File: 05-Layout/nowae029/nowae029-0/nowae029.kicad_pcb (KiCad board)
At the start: 2 copper layers, 100 x 99.9 mm, 160 parts, among them P101 COMM_3, P102 SUPPLY_3, P103 COMM_4, P104 SUPPLY_4, P201 DEBUG, P401 BATTERY, P501 632722110112, P502 UART, Q701 BCW68GLT1G, U201 STM32L073CBT6, U301 TCA9554PWR, U302 TCA9554PWR, U401 TLV70233DBV, U501 FT230XS, U601 TCA9554PWR, U602 TCA9554PWR, Y201 32768

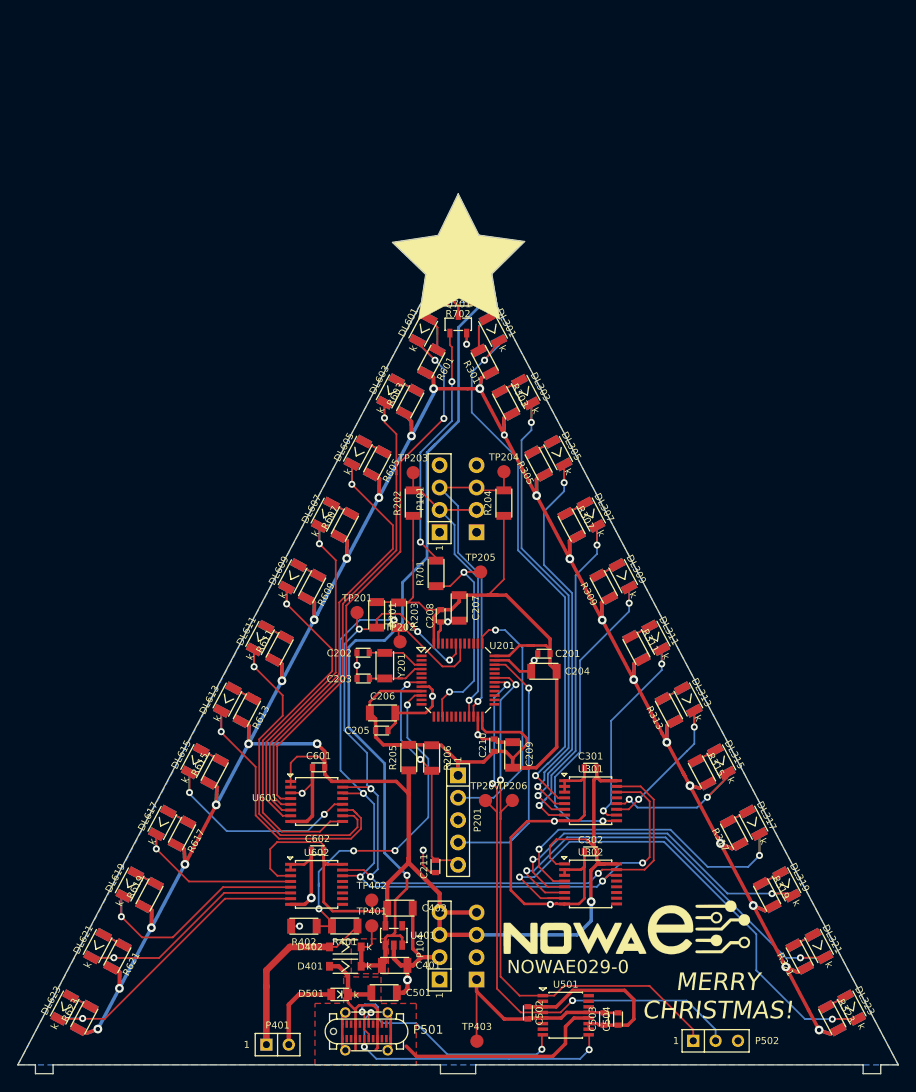
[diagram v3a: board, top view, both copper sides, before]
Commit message: Added fiducial marker
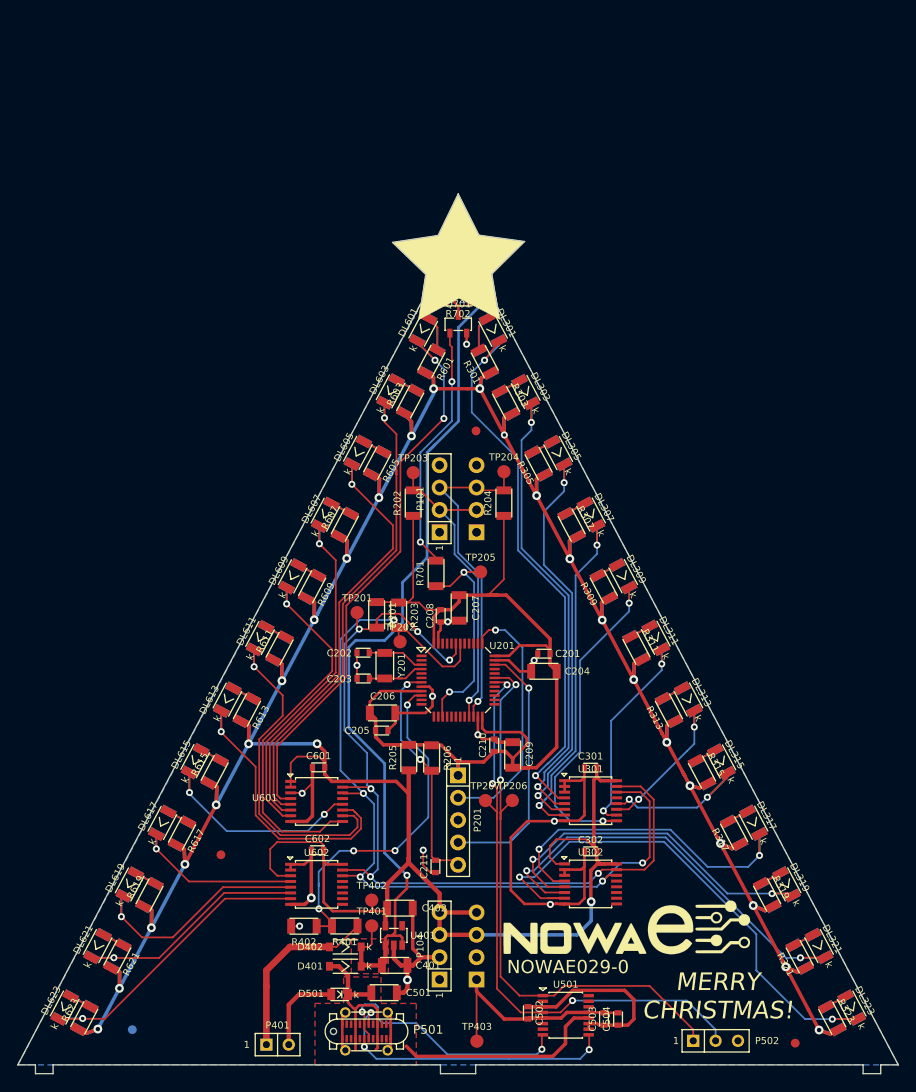
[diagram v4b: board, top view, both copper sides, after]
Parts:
- added VAL**: FIDUCIALMARK_1MM_3MM, MECHANICAL:FIDUCIALMARK_1MM_3MM, B.Cu at (63.0, 145.0)
- added VAL**: FIDUCIALMARK_1MM_3MM, MECHANICAL:FIDUCIALMARK_1MM_3MM, F.Cu at (102.0, 77.0)
- added VAL**: FIDUCIALMARK_1MM_3MM, MECHANICAL:FIDUCIALMARK_1MM_3MM, F.Cu at (73.1, 125.1)
- added VAL**: FIDUCIALMARK_1MM_3MM, MECHANICAL:FIDUCIALMARK_1MM_3MM, F.Cu at (138.3, 146.5)
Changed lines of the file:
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@@
     (tracks 1165)
     (zones 0)
-    (modules 160)
+    (modules 164)
     (nets 156)
   )
@@
     (add_net "Net-(U602-Pad13)")
   )
+  (module MECHANICAL:FIDUCIALMARK_1MM_3MM (layer B.Cu)
+    (at 63 145)
+    (descr "Fiducial Copper Top 1mm copper, 3mm mask")
+    (attr virtual)
+    (fp_text reference VAL** (at 0 2.05) (layer B.SilkS) hide
+      (effects (font (size 0.8 0.8) (thickness 0.15)) (justify mirror))
+    )
+    (fp_text value FIDUCIALMARK_1MM_3MM (at 0 -2.15) (layer B.Fab) hide
+      (effects (font (size 0.8 0.8) (thickness 0.15)) (justify mirror))
+    )
+    (pad "" smd circle (at 0 0) (size 1 1) (layers B.Cu))
+    (pad 1 smd circle (at 0 0) (size 3 3) (layers B.Mask))
+  )
+  (module MECHANICAL:FIDUCIALMARK_1MM_3MM (layer F.Cu)
+    (at 102.04 77)
+    (descr "Fiducial Copper Top 1mm copper, 3mm mask")
+    (attr virtual)
+    (fp_text reference VAL** (at 0 -2.05) (layer F.SilkS) hide
+      (effects (font (size 0.8 0.8) (thickness 0.15)))
+    )
+    (fp_text value FIDUCIALMARK_1MM_3MM (at 0 2.15) (layer F.Fab) hide
+      (effects (font (size 0.8 0.8) (thickness 0.15)))
+    )
+    (pad "" smd circle (at 0 0) (size 1 1) (layers F.Cu))
+    (pad 1 smd circle (at 0 0) (size 3 3) (layers F.Mask))
+  )
+  (module MECHANICAL:FIDUCIALMARK_1MM_3MM (layer F.Cu)
+    (at 73.07 125.14)
+    (descr "Fiducial Copper Top 1mm copper, 3mm mask")
+    (attr virtual)
+    (fp_text reference VAL** (at 0 -2.05) (layer F.SilkS) hide
+      (effects (font (size 0.8 0.8) (thickness 0.15)))
+    )
+    (fp_text value FIDUCIALMARK_1MM_3MM (at 0 2.15) (layer F.Fab) hide
+      (effects (font (size 0.8 0.8) (thickness 0.15)))
+    )
+    (pad "" smd circle (at 0 0) (size 1 1) (layers F.Cu))
+    (pad 1 smd circle (at 0 0) (size 3 3) (layers F.Mask))
+  )
+  (module MECHANICAL:FIDUCIALMARK_1MM_3MM (layer F.Cu)
+    (at 138.29 146.53)
+    (descr "Fiducial Copper Top 1mm copper, 3mm mask")
+    (attr virtual)
+    (fp_text reference VAL** (at 0 -2.05) (layer F.SilkS) hide
+      (effects (font (size 0.8 0.8) (thickness 0.15)))
+    )
+    (fp_text value FIDUCIALMARK_1MM_3MM (at 0 2.15) (layer F.Fab) hide
+      (effects (font (size 0.8 0.8) (thickness 0.15)))
+    )
+    (pad "" smd circle (at 0 0) (size 1 1) (layers F.Cu))
+    (pad 1 smd circle (at 0 0) (size 3 3) (layers F.Mask))
+  )
   (module LOGO:LOGO_NOWAE_30MM_FSILK (layer F.Cu)

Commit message: PCB End! TODO: production documents.
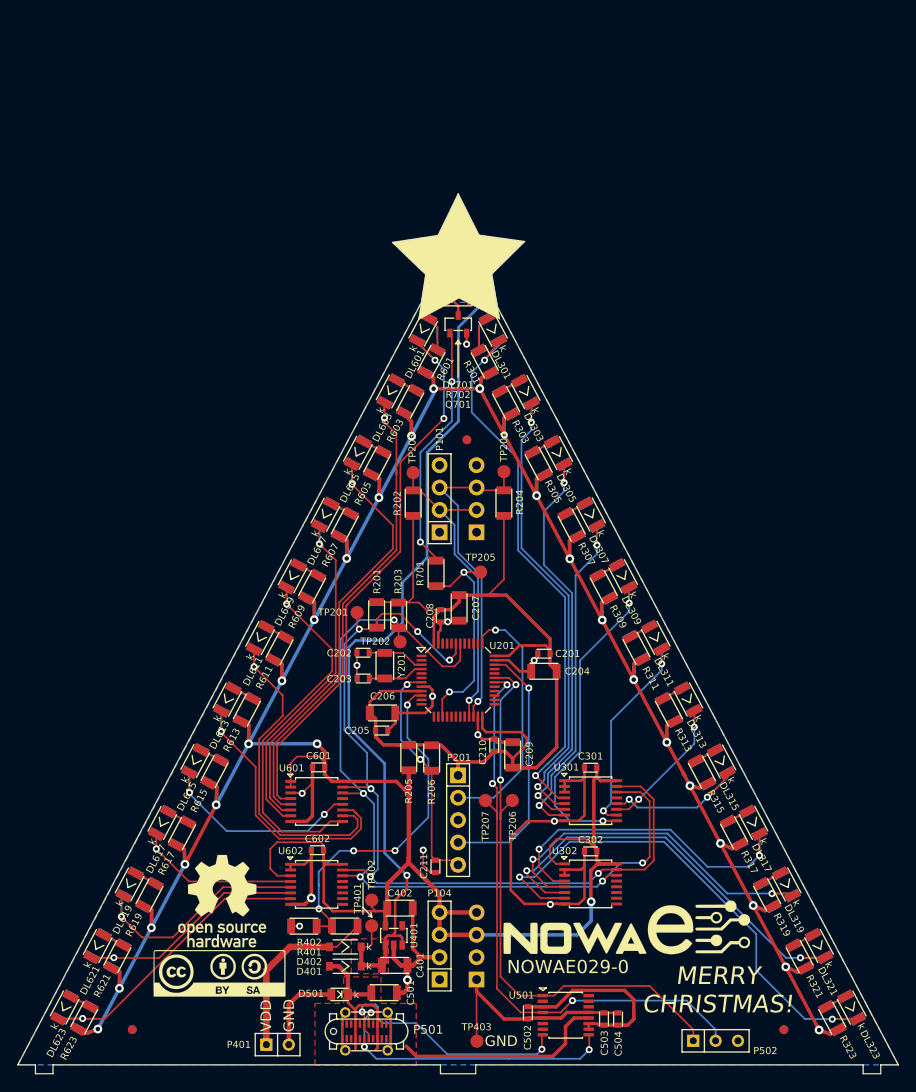
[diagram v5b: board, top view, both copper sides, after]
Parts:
- added G***: LOGO, EXTLOGO:LOGO_OSH_10MM_FSILK, F.Cu at (73.2, 130.4)
- added G***: LOGO, EXTLOGO:LOGO_CC-BY-SA_15MM_FSILK, F.Cu at (72.9, 138.6)
- added VAL**: FIDUCIALMARK_1MM_3MM, MECHANICAL:FIDUCIALMARK_1MM_3MM, B.Cu at (101.0, 78.0)
- added VAL**: FIDUCIALMARK_1MM_3MM, MECHANICAL:FIDUCIALMARK_1MM_3MM, B.Cu at (137.0, 145.0)
- moved VAL** 22.3 mm to (63.0, 145.0)
- moved VAL** 2.00 mm to (137.0, 145.0)
- moved VAL** 1.44 mm to (101.0, 78.0)
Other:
- board text added: "GND"
- board text added: "VDD"

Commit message: small fix
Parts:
- moved C501 20.0 mm to (91.6, 120.8)
- moved D401 20.0 mm to (87.2, 117.8)
- moved DL620 20.0 mm to (62.7, 108.5)
- moved DL623 20.0 mm to (55.3, 122.5)
- moved R619 20.0 mm to (65.0, 109.7)
- moved R620 20.0 mm to (65.0, 109.7)
- moved TP401 20.0 mm to (90.2, 113.2)
- moved U401 20.0 mm to (92.7, 114.3)
- moved U501 20.0 mm to (112.2, 123.4)
- moved DL301 20.0 mm to (104.0, 45.5)
- moved DL305 20.0 mm to (111.4, 59.5)
- moved DL306 20.0 mm to (111.4, 59.5)
- moved DL602 20.0 mm to (96.0, 45.5)
- moved DL603 20.0 mm to (92.3, 52.5)
- moved DL604 20.0 mm to (92.3, 52.5)
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
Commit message: Small fix
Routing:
- net /Branch2/B2_LINE3: track 50.9 -> 48.5 mm
- net /Branch2/B2_LINE6: track 38.4 -> 37.2 mm
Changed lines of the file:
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@@
-(kicad_pcb (version 20171130) (host pcbnew "(5.1.6-0-10_14)")
+(kicad_pcb (version 20171130) (host pcbnew "(5.1.4-0-10_14)")
   (general
     (thickness 1.6)
@@
   (segment (start 95.240734 52.409726) (end 93.020734 51.229726) (width 0.2) (layer B.Cu) (net 55))
   (segment (start 87.94 63.06) (end 87.94 60.77) (width 0.2) (layer F.Cu) (net 56))
-  (via (at 87.94 63.06) (size 0.8) (drill 0.4) (layers F.Cu B.Cu) (net 56) (status 1000000))
+  (via (at 87.94 63.06) (size 0.8) (drill 0.4) (layers F.Cu B.Cu) (net 56))
   (segment (start 87.94 63.06) (end 87.94 60.76) (width 0.2) (layer B.Cu) (net 56))
-  (segment (start 86.50498 76.47502) (end 92.59999 70.38001) (width 0.2) (layer F.Cu) (net 56))
-  (segment (start 86.50498 84.623624) (end 86.50498 76.47502) (width 0.2) (layer F.Cu) (net 56))
+  (segment (start 89.7 64.82) (end 87.94 63.06) (width 0.2) (layer F.Cu) (net 56))
+  (segment (start 89.7 73.28) (end 89.7 64.82) (width 0.2) (layer F.Cu) (net 56))
+  (segment (start 86.50498 76.47502) (end 89.7 73.28) (width 0.2) (layer F.Cu) (net 56))
+  (segment (start 79.995 100.055) (end 78.62 98.68) (width 0.2) (layer F.Cu) (net 56))
   (segment (start 78.62 92.508604) (end 86.50498 84.623624) (width 0.2) (layer F.Cu) (net 56))
-  (segment (start 92.59999 70.38001) (end 92.59999 67.71999) (width 0.2) (layer F.Cu) (net 56))
+  (segment (start 86.50498 84.623624) (end 86.50498 76.47502) (width 0.2) (layer F.Cu) (net 56))
   (segment (start 78.62 98.68) (end 78.62 92.508604) (width 0.2) (layer F.Cu) (net 56))
   (segment (start 80.99 100.055) (end 79.995 100.055) (width 0.2) (layer F.Cu) (net 56))
-  (segment (start 79.995 100.055) (end 78.62 98.68) (width 0.2) (layer F.Cu) (net 56))
-  (segment (start 92.59999 67.71999) (end 87.94 63.06) (width 0.2) (layer F.Cu) (net 56))
   (segment (start 89.301468 58.209452) (end 91.500734 59.379726) (width 0.2) (layer F.Cu) (net 57))
   (segment (start 91.490734 59.369726) (end 89.301468 58.199452) (width 0.2) (layer B.Cu) (net 58))
@@
   (segment (start 84.110734 73.429726) (end 81.880734 72.229726) (width 0.2) (layer B.Cu) (net 64))
   (segment (start 76.834266 83.784266) (end 76.834266 81.806011) (width 0.2) (layer F.Cu) (net 65))
-  (segment (start 80.08 89.351509) (end 80.08 87.03) (width 0.2) (layer F.Cu) (net 65))
-  (segment (start 77.41 92.021509) (end 80.08 89.351509) (width 0.2) (layer F.Cu) (net 65))
-  (segment (start 77.41 100.495699) (end 77.41 92.021509) (width 0.2) (layer F.Cu) (net 65))
-  (segment (start 88.135 100.705) (end 88.58 101.15) (width 0.2) (layer F.Cu) (net 65))
-  (segment (start 80.08 87.03) (end 76.834266 83.784266) (width 0.2) (layer F.Cu) (net 65))
+  (via (at 76.834266 83.784266) (size 0.8) (drill 0.4) (layers F.Cu B.Cu) (net 65))
+  (segment (start 76.834266 81.815274) (end 76.839266 81.810274) (width 0.2) (layer B.Cu) (net 65))
+  (segment (start 76.834266 83.784266) (end 76.834266 81.815274) (width 0.2) (layer B.Cu) (net 65))
+  (segment (start 78.6 85.55) (end 76.834266 83.784266) (width 0.2) (layer F.Cu) (net 65))
+  (segment (start 79.824311 102.91001) (end 77.41 100.495699) (width 0.2) (layer F.Cu) (net 65))
   (segment (start 87.67999 102.91001) (end 79.824311 102.91001) (width 0.2) (layer F.Cu) (net 65))
   (segment (start 88.58 102.01) (end 87.67999 102.91001) (width 0.2) (layer F.Cu) (net 65))
-  (segment (start 79.824311 102.91001) (end 77.41 100.495699) (width 0.2) (layer F.Cu) (net 65))
+  (segment (start 78.6 90.831509) (end 78.6 85.55) (width 0.2) (layer F.Cu) (net 65))
+  (segment (start 77.41 92.021509) (end 78.6 90.831509) (width 0.2) (layer F.Cu) (net 65))
   (segment (start 88.58 101.15) (end 88.58 102.01) (width 0.2) (layer F.Cu) (net 65))
+  (segment (start 77.41 100.495699) (end 77.41 92.021509) (width 0.2) (layer F.Cu) (net 65))
+  (segment (start 88.135 100.705) (end 88.58 101.15) (width 0.2) (layer F.Cu) (net 65))
   (segment (start 86.89 100.705) (end 88.135 100.705) (width 0.2) (layer F.Cu) (net 65))
-  (via (at 76.834266 83.784266) (size 0.8) (drill 0.4) (layers F.Cu B.Cu) (net 65))
-  (segment (start 76.834266 81.815274) (end 76.839266 81.810274) (width 0.2) (layer B.Cu) (net 65))
-  (segment (start 76.834266 83.784266) (end 76.834266 81.815274) (width 0.2) (layer B.Cu) (net 65))
   (segment (start 78.195734 79.245463) (end 80.410734 80.429726) (width 0.2) (layer F.Cu) (net 66))
   (segment (start 80.394997 80.434726) (end 78.200734 79.249726) (width 0.2) (layer B.Cu) (net 67))
